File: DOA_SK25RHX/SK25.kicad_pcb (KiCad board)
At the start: 2 copper layers, 29.2 x 29.2 mm, 44 parts, among them J1 Imput-, J2 Input+, J3 V+, J4 Output, J5 V-, J6 GND, Q1 BC560C, Q10 BD140, Q2 KSA992, Q3 KSA992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

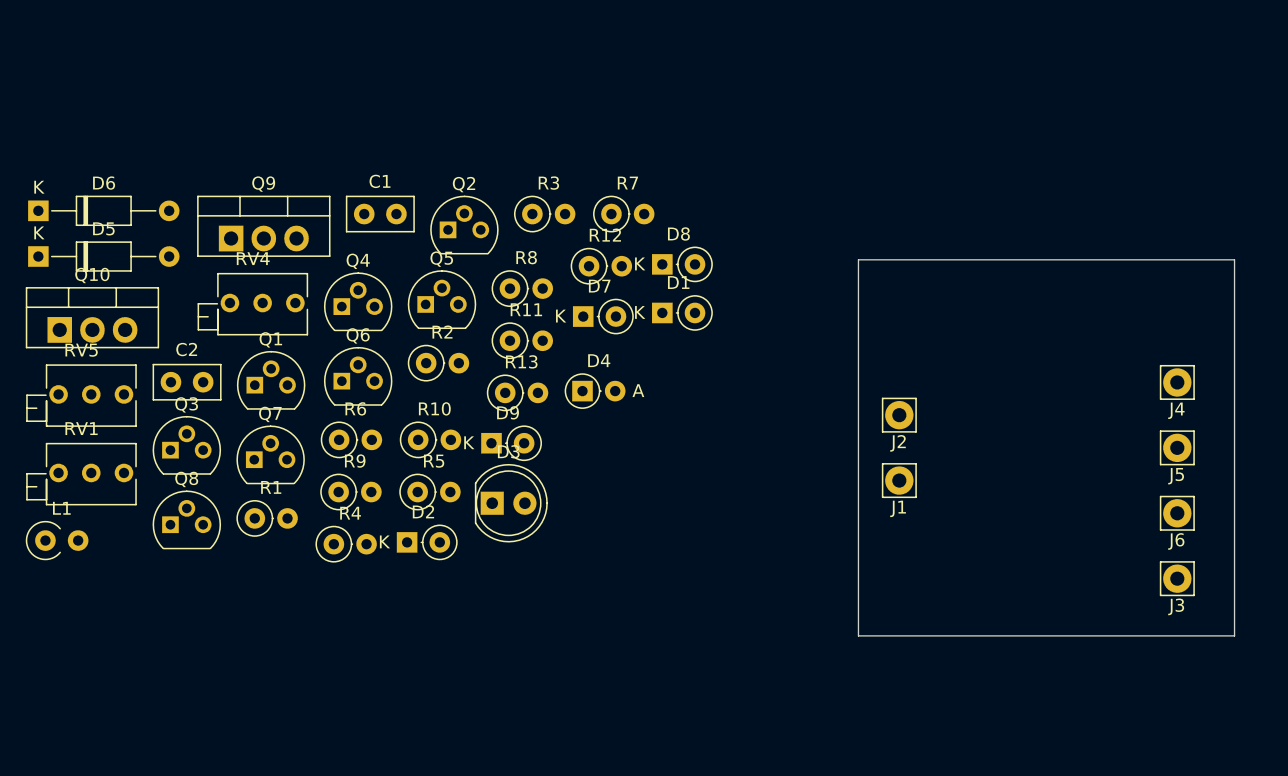
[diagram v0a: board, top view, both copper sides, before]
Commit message: abandoned layout. just TAC schematics for DOA socket
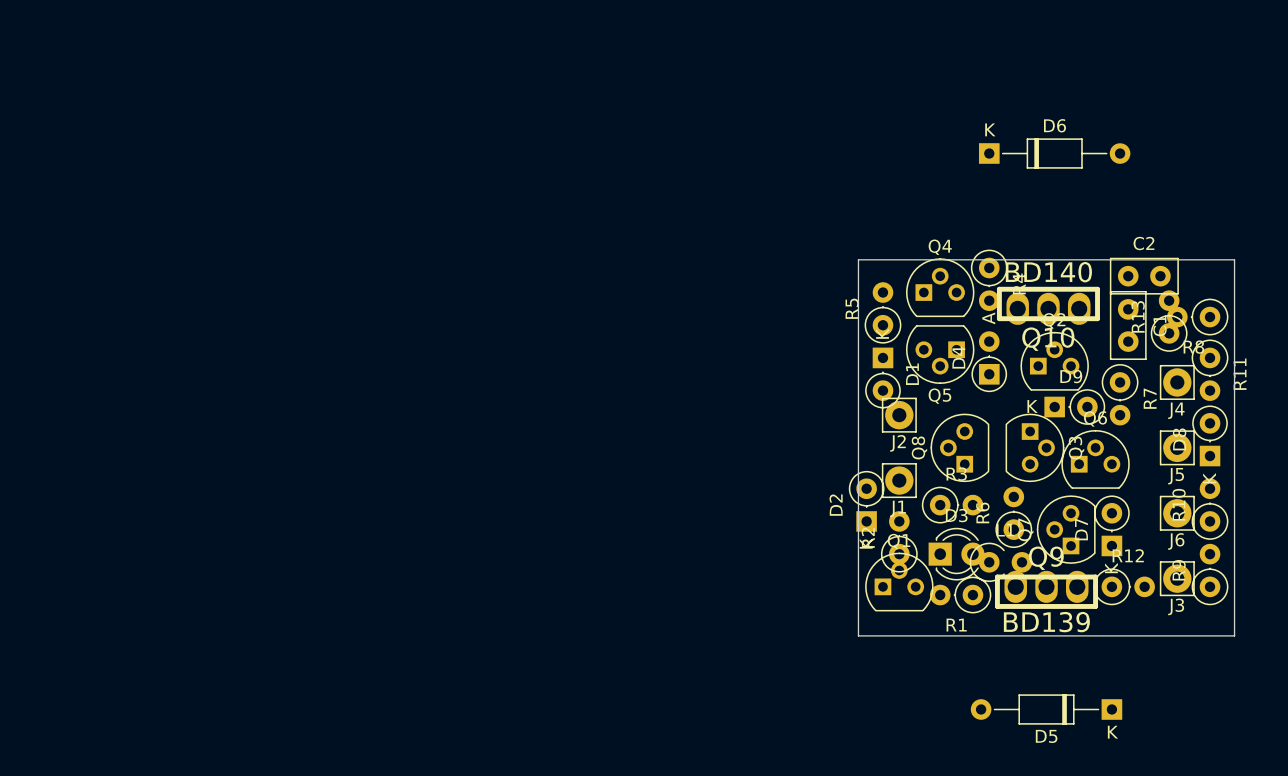
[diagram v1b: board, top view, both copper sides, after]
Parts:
- removed RV1, RV4, RV5: 2k, Potentiometer_THT:Potentiometer_Bourns_3266Z_Horizontal
- D3: footprint LED_THT:LED_D5.0mm -> LED_THT:LED_D3.0mm
- Q10, Q9: footprint Package_TO_SOT_THT:TO-220-3_Vertical -> TAC:to225_std
- R1, R4, R5: value 470R -> 2k2
- moved D5 90.5 mm to (163.8, 115.6), turned to 180 degrees
- moved Q10 76.8 mm to (158.9, 84.5)
- moved C2 74.8 mm to (165.1, 81.9)
- moved D6 74.0 mm to (154.3, 72.4)
- moved L1 73.3 mm to (154.3, 104.1)
- moved Q9 68.9 mm to (158.8, 106.0), turned to 180 degrees
- moved R9 68.1 mm to (171.4, 106.0), turned to 90 degrees
- moved Q3 66.8 mm to (157.5, 94.0), turned to 270 degrees
- moved Q7 63.8 mm to (160.7, 102.9), turned to 90 degrees
- moved Q8 61.9 mm to (152.4, 96.5), turned to 90 degrees
- moved R10 61.8 mm to (171.4, 101.0), turned to 90 degrees
- moved C1 59.8 mm to (165.1, 84.5), turned to 270 degrees
- moved Q6 57.6 mm to (161.3, 96.5)
- moved R1 56.1 mm to (153.0, 106.7), turned to 180 degrees
- moved R4 55.2 mm to (154.3, 81.3), turned to 270 degrees
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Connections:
- R1 pad 2: Net-(R1-Pad2) -> Net-(Q1-Pad3)
- R4 pad 2: Net-(R4-Pad2) -> Net-(C2-Pad2)
- R5 pad 2: Net-(R5-Pad2) -> Net-(C2-Pad2)

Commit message: status before using KiCad 6.0
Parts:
- moved J1 1.27 mm to (148.6, 97.8)
- moved J2 1.27 mm to (148.6, 92.7)
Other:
- board size 29.2 x 29.2 mm -> 30.5 x 30.5 mm
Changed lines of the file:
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@@
   )
   (module Connector_Pin:Pin_D1.1mm_L8.5mm_W2.5mm_FlatFork (layer F.Cu)
-    (at 147.32 97.79)
+    (at 148.59 97.79)
     (descr "solder Pin_ with flat fork, hole diameter 1.1mm, length 8.5mm, width 2.5mm")
     (tags "solder Pin_ with flat fork")
@@
   )
   (module Connector_Pin:Pin_D1.1mm_L8.5mm_W2.5mm_FlatFork (layer F.Cu)
-    (at 147.32 92.71)
+    (at 148.59 92.71)
     (descr "solder Pin_ with flat fork, hole diameter 1.1mm, length 8.5mm, width 2.5mm")
     (tags "solder Pin_ with flat fork")
@@
     )
   )
-  (gr_line (start 144.145 80.645) (end 173.355 80.645) (layer Edge.Cuts) (width 0.05))
-  (gr_line (start 144.145 109.855) (end 144.145 80.645) (layer Edge.Cuts) (width 0.05))
-  (gr_line (start 173.355 109.855) (end 144.145 109.855) (layer Edge.Cuts) (width 0.05))
-  (gr_line (start 173.355 80.645) (end 173.355 109.855) (layer Edge.Cuts) (width 0.05))
+  (gr_line (start 143.51 110.49) (end 173.99 110.49) (layer Edge.Cuts) (width 0.05))
+  (gr_line (start 143.51 80.01) (end 143.51 110.49) (layer Edge.Cuts) (width 0.05))
+  (gr_line (start 173.99 80.01) (end 143.51 80.01) (layer Edge.Cuts) (width 0.05))
+  (gr_line (start 173.99 110.49) (end 173.99 80.01) (layer Edge.Cuts) (width 0.05))
 )

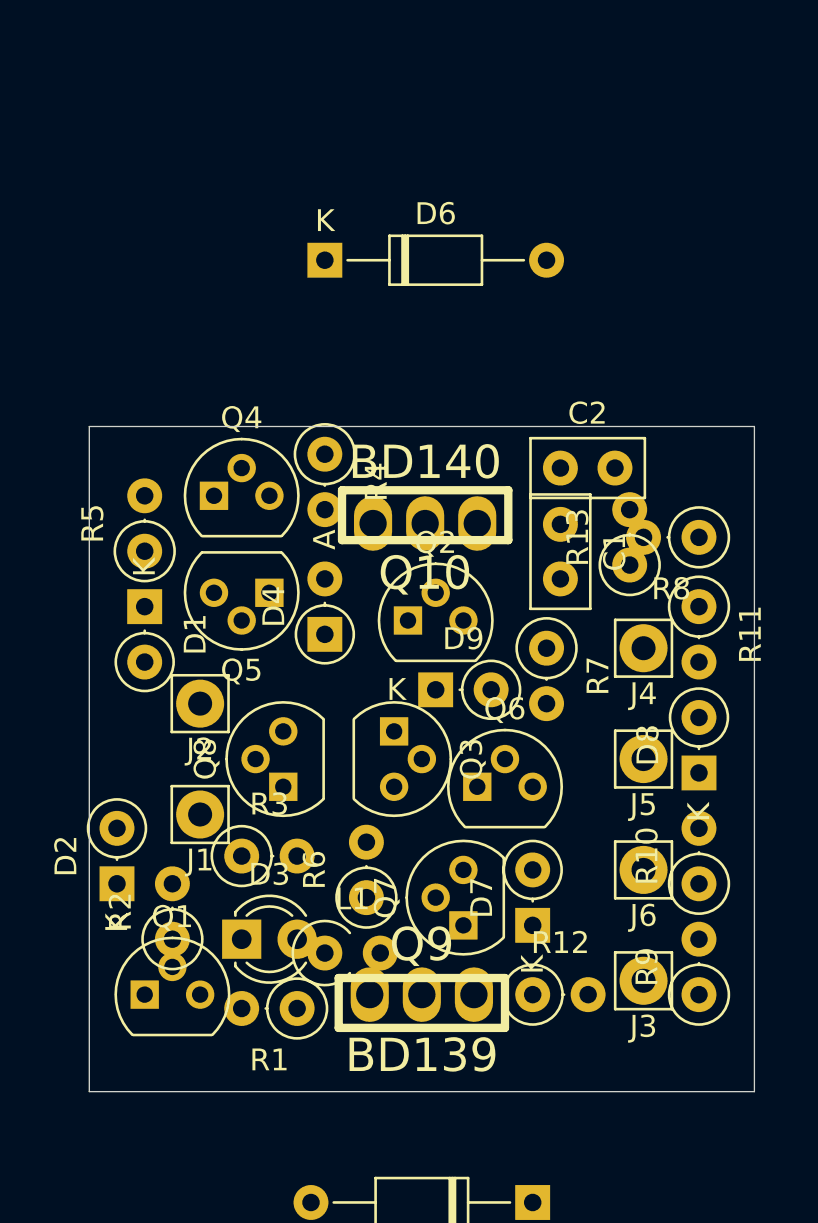
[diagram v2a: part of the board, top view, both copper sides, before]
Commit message: expanded PBC borders to fit with TAC 270D mod clearance
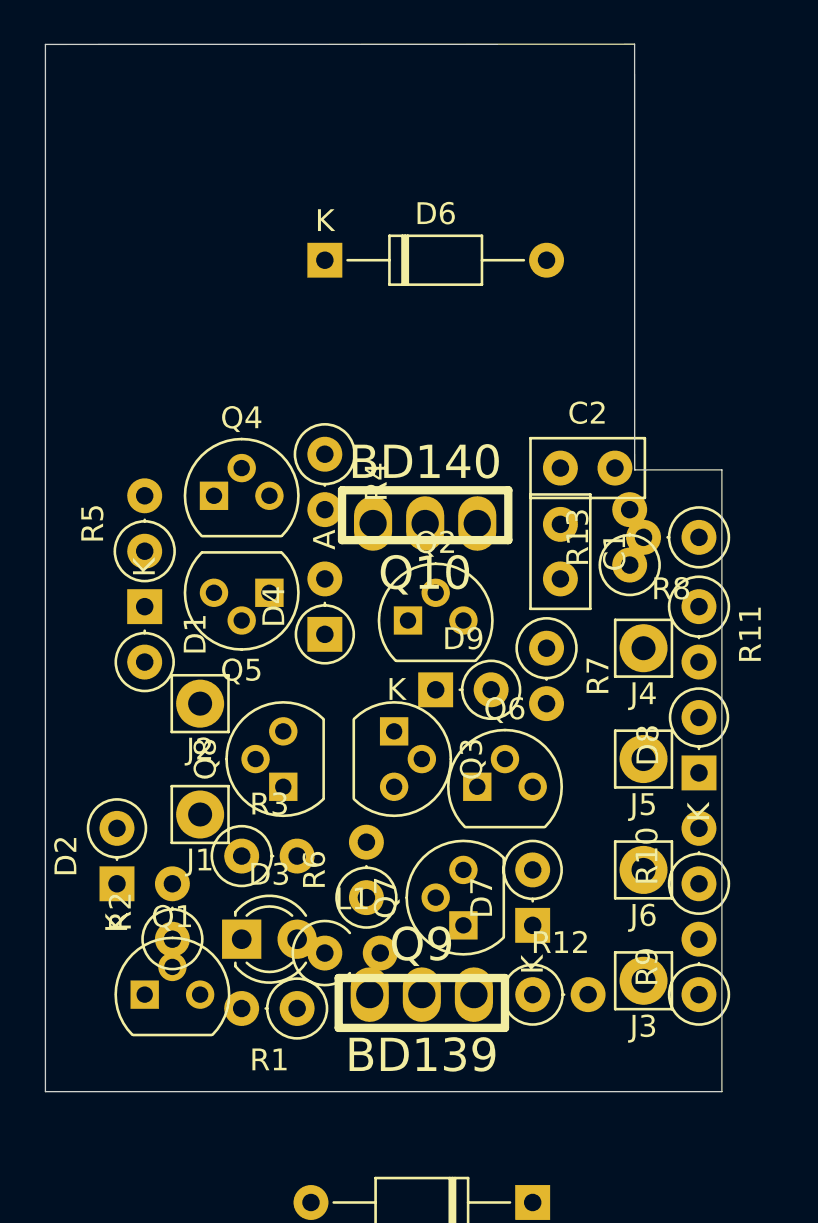
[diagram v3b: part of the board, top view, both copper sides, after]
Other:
- board size 30.5 x 30.5 mm -> 31 x 48 mm
- net class Default removed

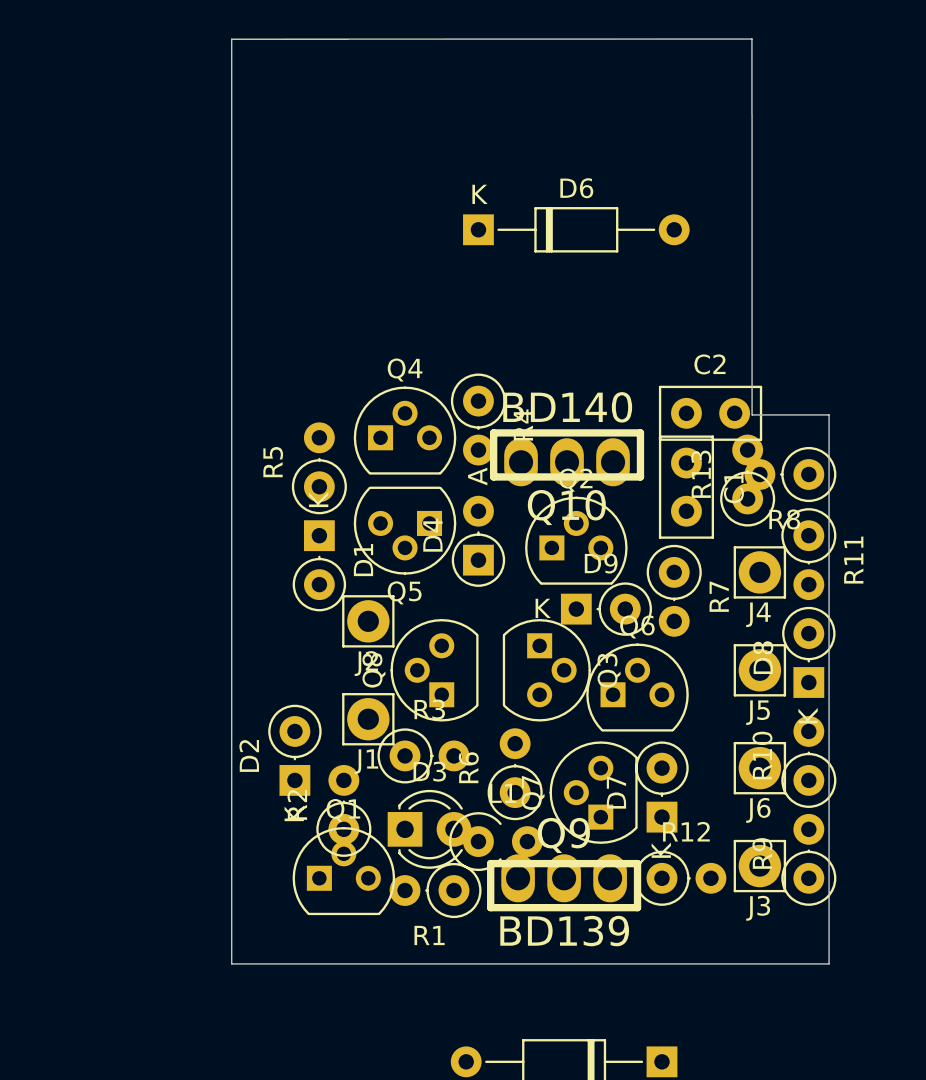
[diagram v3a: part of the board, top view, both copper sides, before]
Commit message: complete plausible placement
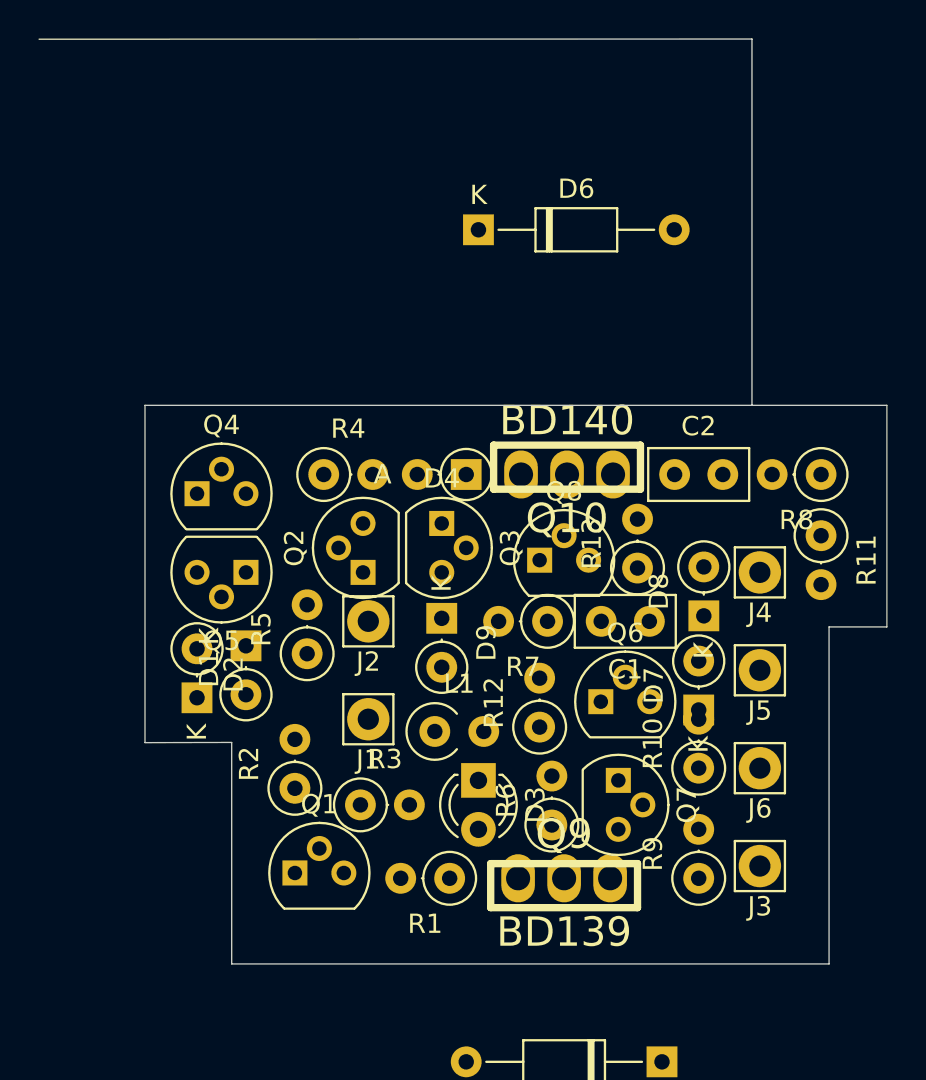
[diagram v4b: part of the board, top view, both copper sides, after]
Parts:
- moved R12 10.1 mm to (157.5, 98.2), turned to 90 degrees
- moved Q4 9.96 mm to (139.7, 86.1)
- moved Q2 9.88 mm to (148.3, 90.2), turned to 90 degrees
- moved Q5 9.86 mm to (142.2, 90.2)
- moved R4 8.89 mm to (146.3, 85.1), turned to 0 degrees
- moved R5 8.69 mm to (145.4, 94.4)
- moved Q8 8.64 mm to (157.5, 89.5), turned to 0 degrees
- moved C1 8.44 mm to (163.2, 92.7), turned to 180 degrees
- moved Q3 8.13 mm to (152.4, 87.6)
- moved R7 7.05 mm to (157.9, 92.7), turned to 180 degrees
- moved D9 7.00 mm to (152.4, 92.6), turned to -90 degrees
- moved D1 6.87 mm to (142.2, 94.0)
- moved R13 6.75 mm to (162.6, 89.9)
- moved D2 6.65 mm to (139.7, 96.7)
- moved D8 6.46 mm to (166.0, 92.4)
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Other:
- board size 31 x 48 mm -> 44 x 48 mm

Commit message: added PCB serial No
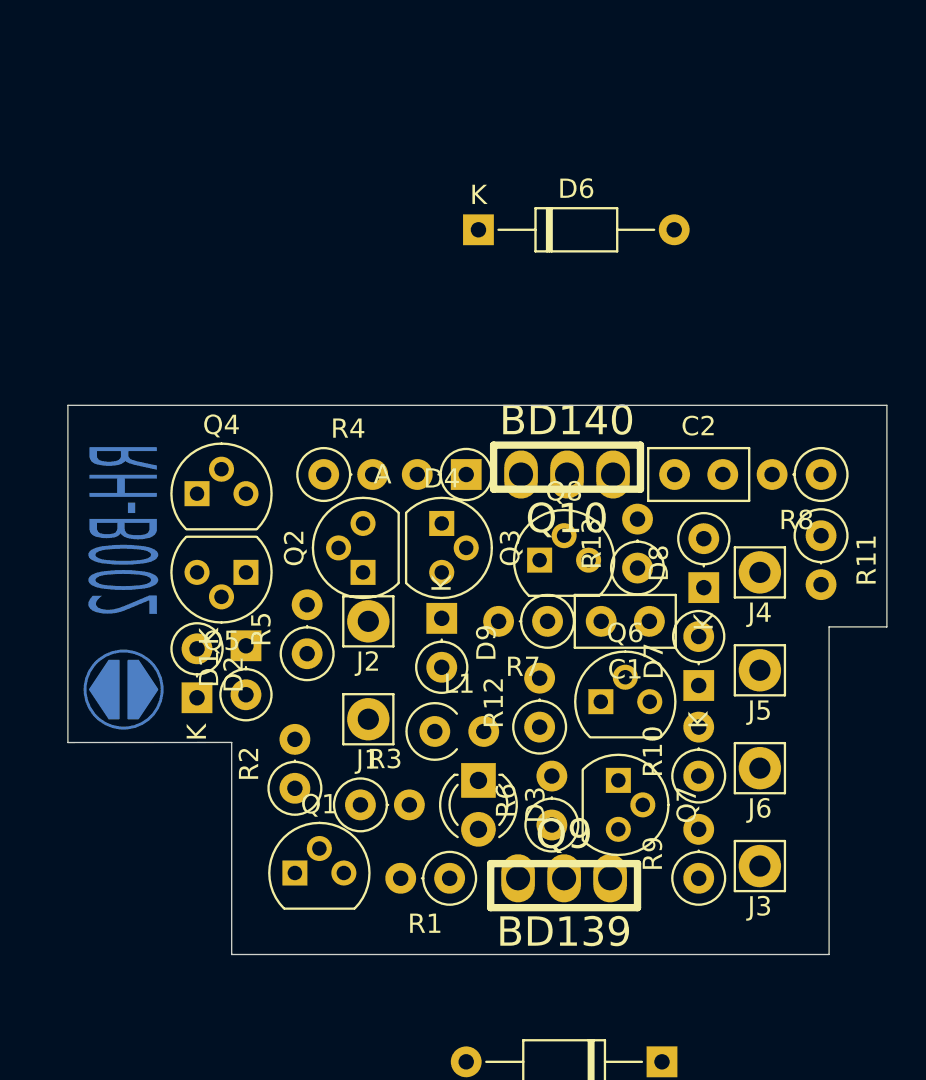
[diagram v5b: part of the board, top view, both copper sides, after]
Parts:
- moved D8 1.47 mm to (166.0, 91.0)
- moved D7 1.27 mm to (165.7, 96.0)
- moved R10 0.41 mm to (165.7, 100.7)
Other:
- board size 44 x 48 mm -> 42.5 x 28.5 mm
- board text added: "RH-B002"
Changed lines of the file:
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@@
   )
   (footprint "Diode_THT:D_DO-35_SOD27_P2.54mm_Vertical_KathodeUp" (layer "F.Cu")
-    (at 165.735 97.310686 90)
+    (at 165.735 96.040686 90)
     (descr "Diode, DO-35_SOD27 series, Axial, Vertical, pin pitch=2.54mm, , length*diameter=4*2mm^2, , http://www.diodes.com/_files/packages/DO-35.pdf")
     (tags "Diode DO-35_SOD27 series Axial Vertical pin pitch 2.54mm  length 4mm diameter 2mm")
@@
   )
   (footprint "Diode_THT:D_DO-35_SOD27_P2.54mm_Vertical_KathodeUp" (layer "F.Cu")
-    (at 166 92.425686 90)
+    (at 166 90.960686 90)
     (descr "Diode, DO-35_SOD27 series, Axial, Vertical, pin pitch=2.54mm, , length*diameter=4*2mm^2, , http://www.diodes.com/_files/packages/DO-35.pdf")
     (tags "Diode DO-35_SOD27 series Axial Vertical pin pitch 2.54mm  length 4mm diameter 2mm")
@@
   )
   (footprint "Resistor_THT:R_Axial_DIN0207_L6.3mm_D2.5mm_P2.54mm_Vertical" (layer "F.Cu")
-    (at 165.735 100.33 90)
+    (at 165.735 100.74 90)
     (descr "Resistor, Axial_DIN0207 series, Axial, Vertical, pin pitch=2.54mm, 0.25W = 1/4W, length*diameter=6.3*2.5mm^2, http://cdn-reichelt.de/documents/datenblatt/B400/1_4W%23YAG.pdf")
     (tags "Resistor Axial_DIN0207 series Axial Vertical pin pitch 2.54mm 0.25W = 1/4W length 6.3mm diameter 2.5mm")
@@
     )
   )
-  (gr_line (start 141.5 110.49) (end 172.5 110.49) (layer "Edge.Cuts") (width 0.05))
-  (gr_line (start 141.5 99) (end 141.5 110.49) (layer "Edge.Cuts") (width 0.05))
-  (gr_line (start 137 99.005) (end 137 81.5) (layer "Edge.Cuts") (width 0.05))
-  (gr_line (start 168.5 62.49) (end 131.5 62.5) (layer "Edge.Cuts") (width 0.05))
+  (gr_poly
+    (pts
+      (xy 135.14 94.75)
+      (xy 135.64 94.75)
+      (xy 135.64 97.75)
+      (xy 135.14 97.75)
+      (xy 134.14 96.25)
+    ) (layer "B.Cu") (width 0.1) (fill solid))
+  (gr_poly
+    (pts
+      (xy 136.64 94.75)
+      (xy 137.64 96.25)
+      (xy 136.64 97.75)
+      (xy 136.14 97.75)
+      (xy 136.14 94.75)
+    ) (layer "B.Cu") (width 0.1) (fill solid))
+  (gr_circle (center 135.89 96.25) (end 135.89 94.25) (layer "B.Cu") (width 0.15) (fill none))
+  (gr_line (start 141.5 110) (end 172.5 110) (layer "Edge.Cuts") (width 0.05))
+  (gr_line (start 141.5 99) (end 141.5 110) (layer "Edge.Cuts") (width 0.05))
+  (gr_line (start 133 99) (end 133 81.5) (layer "Edge.Cuts") (width 0.05))
   (gr_line (start 175.5 93) (end 172.5 93) (layer "Edge.Cuts") (width 0.05))
-  (gr_line (start 172.5 110.49) (end 172.5 93) (layer "Edge.Cuts") (width 0.05))
-  (gr_line (start 141.5 98.995) (end 137 99.005) (layer "Edge.Cuts") (width 0.05))
-  (gr_line (start 168.5 81.5) (end 168.5 62.49) (layer "Edge.Cuts") (width 0.05))
+  (gr_line (start 172.5 110) (end 172.5 93) (layer "Edge.Cuts") (width 0.05))
+  (gr_line (start 141.5 98.995) (end 133 99) (layer "Edge.Cuts") (width 0.05))
   (gr_line (start 175.5 93) (end 175.5 81.5) (layer "Edge.Cuts") (width 0.05))
-  (gr_line (start 175.5 81.5) (end 137 81.5) (layer "Edge.Cuts") (width 0.05))
+  (gr_line (start 175.5 81.5) (end 133 81.5) (layer "Edge.Cuts") (width 0.05))
+  (gr_text "RH-B002" (at 136 88 90) (layer "B.Cu")
+    (effects (font (size 3.5 1.5) (thickness 0.35)) (justify mirror))
+  )
 )

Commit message: 2/3 of routing
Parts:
- moved R12 0.90 mm to (156.8, 98.8)
- moved Q6 0.73 mm to (160.0, 96.5)
- moved R7 0.64 mm to (158.5, 92.7)
- moved C1 0.63 mm to (163.8, 92.7)
- moved D7 0.63 mm to (166.4, 96.0)
- moved L1 0.63 mm to (151.4, 98.4)
- moved R13 0.63 mm to (163.2, 89.9)
- moved R3 0.63 mm to (148.8, 102.2)
- moved D4 0.51 mm to (153.7, 84.6)
- moved R4 0.51 mm to (146.3, 84.6)
- moved Q4 0.36 mm to (139.7, 85.7)
- moved Q5 0.36 mm to (142.2, 89.8)
- moved D9 0.25 mm to (152.7, 92.6)
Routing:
- net Net-(D9-Pad2): track 0.00 -> 30.3 mm, vias 0 -> 1
- net Net-(Q3-Pad2): track 0.00 -> 27.3 mm
- net Net-(D4-Pad1): track 0.00 -> 22.0 mm, vias 0 -> 1
- net Net-(D3-Pad2): track 0.00 -> 21.6 mm
- net Net-(D1-Pad1): track 0.00 -> 20.7 mm
- net Net-(D3-Pad1): track 0.00 -> 19.8 mm
- net Net-(D1-Pad2): track 0.00 -> 19.1 mm
- net Net-(L1-Pad2): track 0.00 -> 18.8 mm
- net Net-(C2-Pad2): track 0.00 -> 18.8 mm
- net Net-(C1-Pad1): track 0.00 -> 18.5 mm
- net Net-(L1-Pad1): track 0.00 -> 17.9 mm
- net Net-(D7-Pad2): track 0.00 -> 13.8 mm
- net Net-(D5-Pad2): track 0.00 -> 13.7 mm
- net Net-(Q5-Pad3): track 0.00 -> 9.46 mm
- net Net-(Q1-Pad1): track 0.00 -> 8.79 mm
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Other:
- board size 42.5 x 28.5 mm -> 42.5 x 30 mm
